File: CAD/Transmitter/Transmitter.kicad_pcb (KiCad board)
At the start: 2 copper layers, 193.8 x 67.8 mm, 53 parts

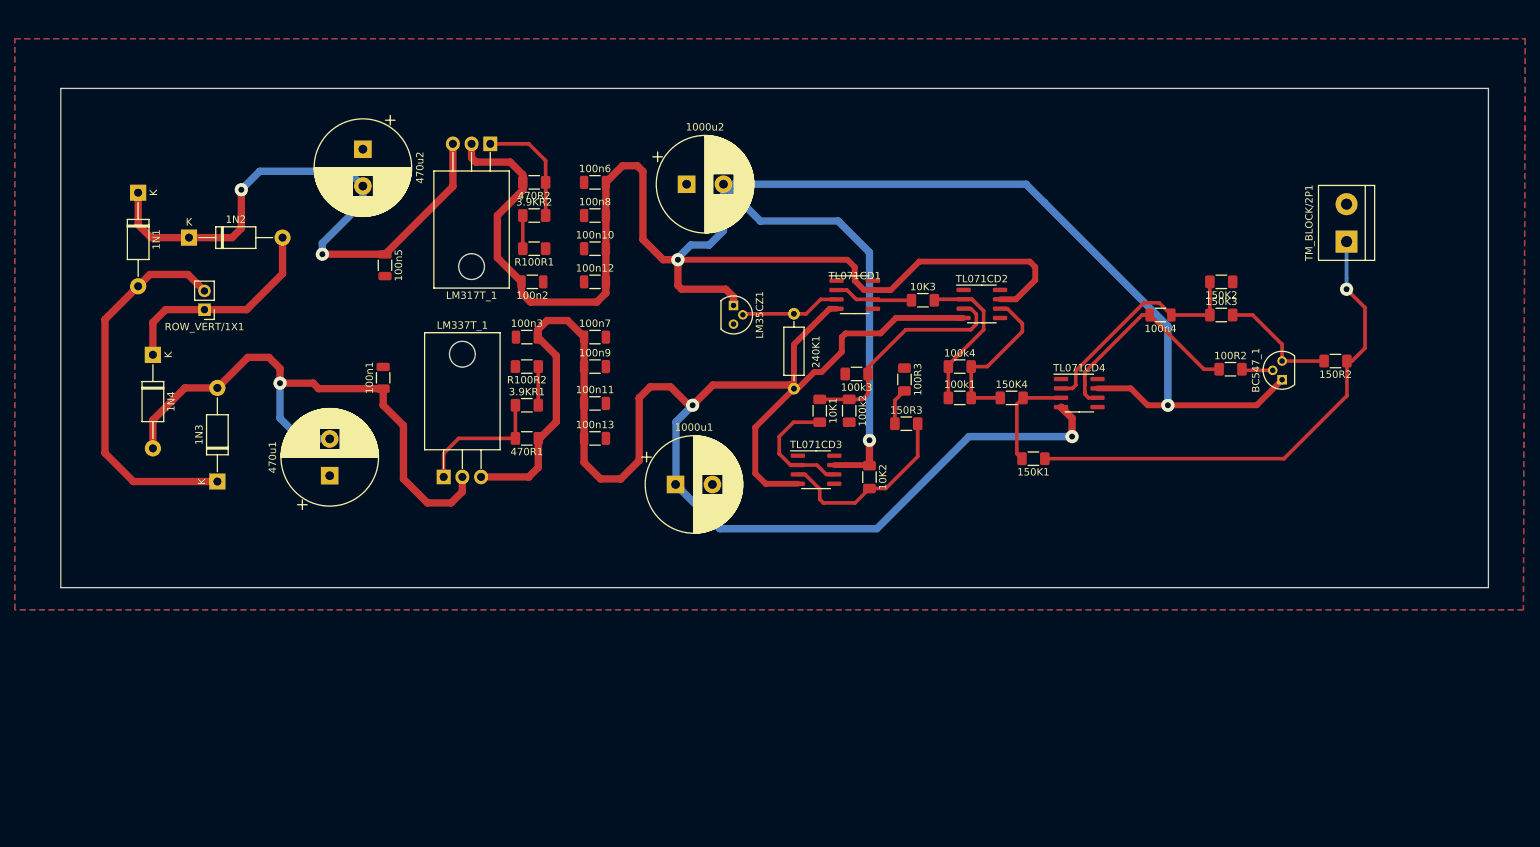
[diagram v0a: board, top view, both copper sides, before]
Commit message: PCB adjusted to the Eurocad size standards
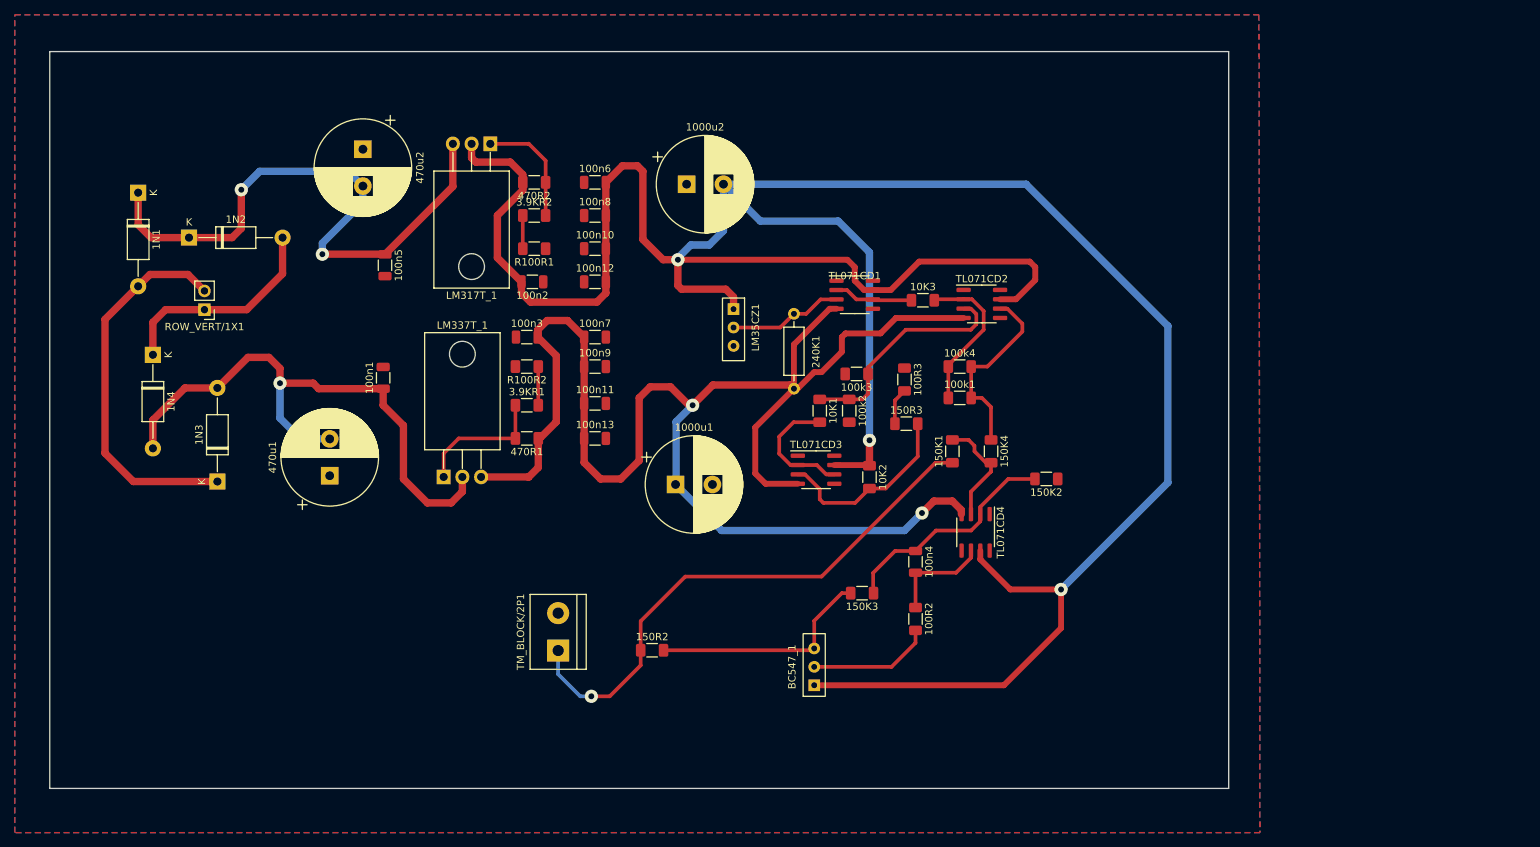
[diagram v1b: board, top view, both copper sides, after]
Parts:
- LM35CZ1: footprint VAMK_IC:TO-92 -> VAMK_ANA:TO-92_2
- moved TM_BLOCK/2P1 120.5 mm to (124.0, 133.0)
- moved 150R2 100.7 mm to (136.8, 133.0), turned to 0 degrees
- moved BC547_1 76.1 mm to (158.8, 138.2)
- moved 150K3 61.7 mm to (165.2, 125.2), turned to 180 degrees
- moved 100R2 54.6 mm to (172.5, 128.8), turned to -90 degrees
- moved 100n4 47.2 mm to (172.5, 121.0), turned to -90 degrees
- moved 150K2 35.8 mm to (190.2, 109.8)
- moved TL071CD4 23.6 mm to (180.7, 117.0), turned to -90 degrees
- moved 150K1 11.0 mm to (177.5, 106.0), turned to 90 degrees
- moved 150K4 7.77 mm to (182.8, 106.0), turned to -90 degrees
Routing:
- net +12V: track 329.7 -> 389.1 mm
- net -12V: track 235.7 -> 213.7 mm
- net Net-(100R2-Pad1): track 29.4 -> 14.1 mm
- net Net-(BC547_1-E): track 16.3 -> 30.8 mm
- net Net-(BC547_1-B): track 4.24 -> 16.8 mm
- net Net-(TM_BLOCK/2P1-Pin_1): track 67.9 -> 74.7 mm
- net Net-(100k1-Pad2): track 22.1 -> 25.8 mm
- net Net-(LM35CZ1-Vout): track 13.6 -> 15.6 mm
- net Net-(TL071CD4-+): track 14.1 -> 15.1 mm
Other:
- board size 193.8 x 67.8 mm -> 160 x 100 mm
